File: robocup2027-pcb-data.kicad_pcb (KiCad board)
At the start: 6 copper layers, 83 x 117 mm, 51 parts, among them M5 Motor_Servo, M6 Motor_Servo, Q1 BPW40, Q2 BPW40, U1 ESP32-DEVKITC-32E

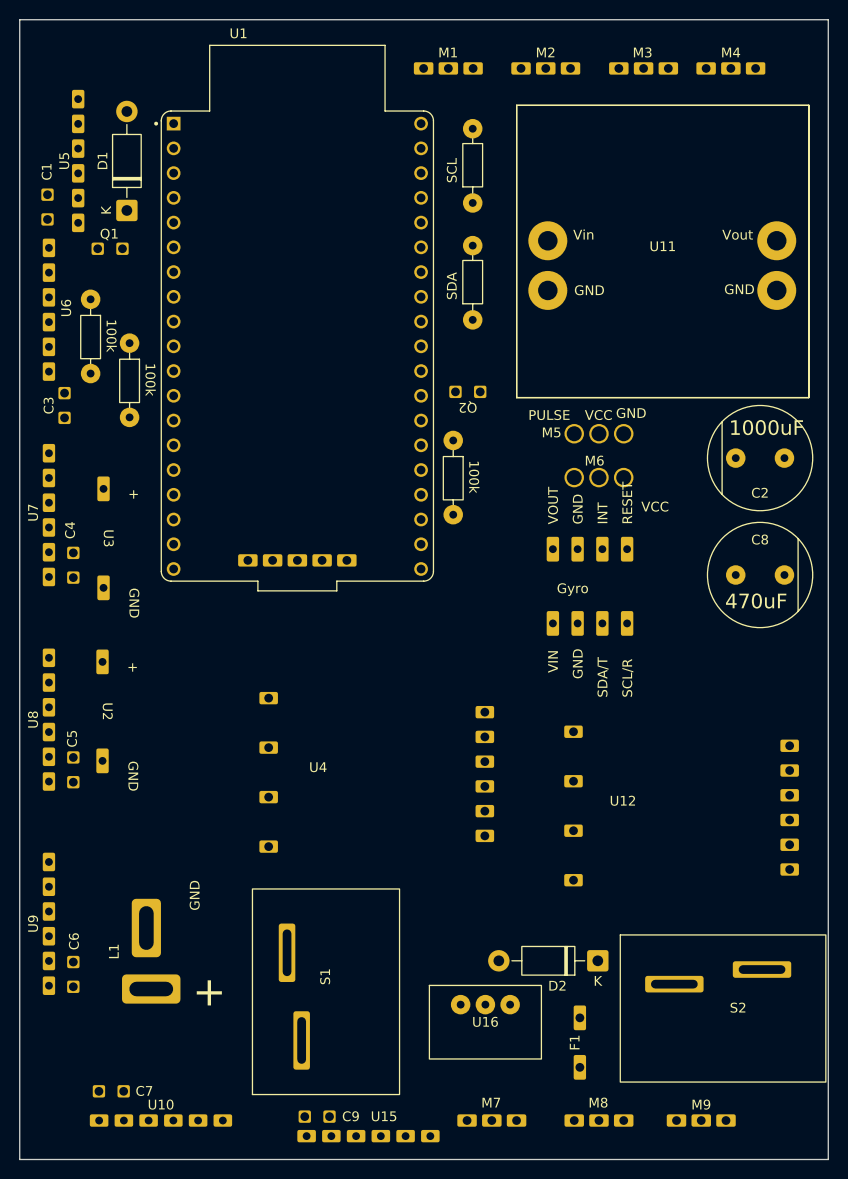
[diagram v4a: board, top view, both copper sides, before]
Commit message: add debug speaker
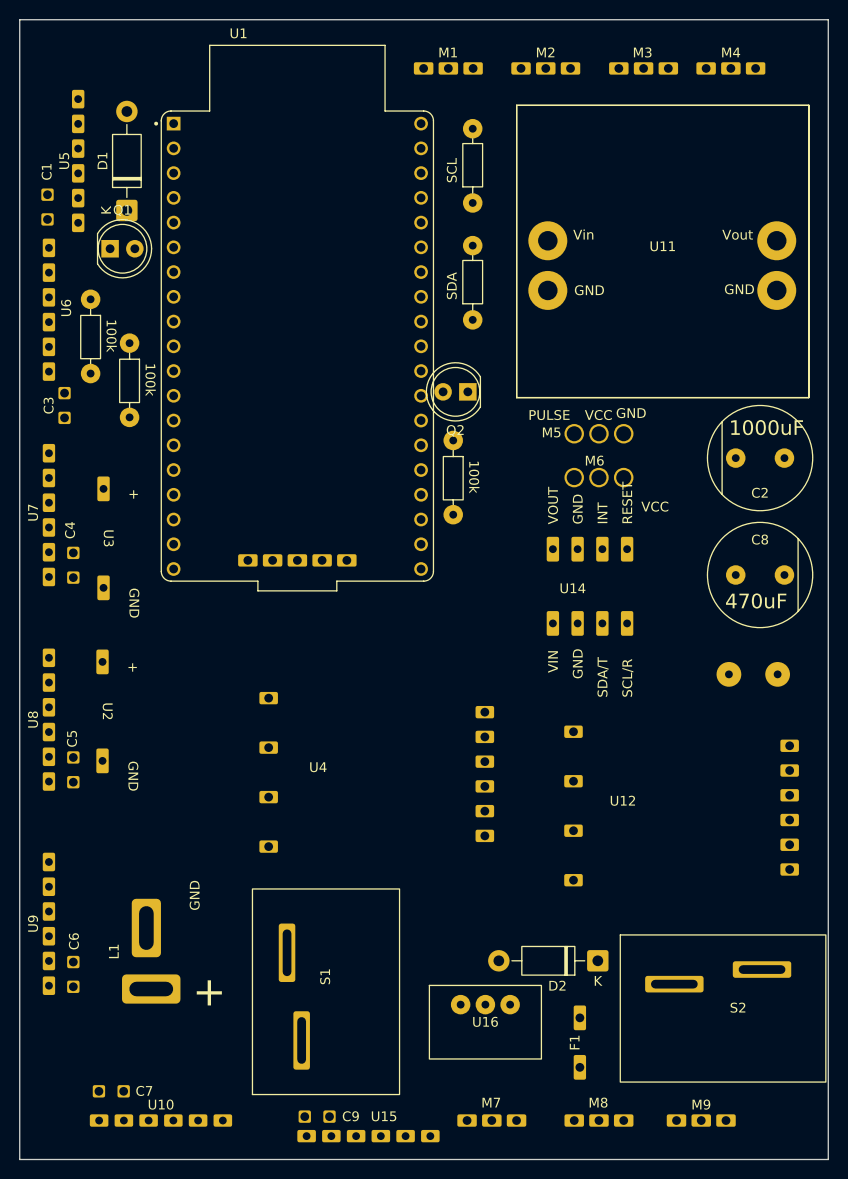
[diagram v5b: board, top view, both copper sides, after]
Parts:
- added U17: ~, robo:PKM13EPYH4000-A0, B.Cu at (165.3, 100.2)
- Q1, Q2: footprint robo:2.54mm_capacitor -> LED_THT:LED_D5.0mm_Clear
- renumbered Gyro to U14
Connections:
- U1 pad J3_15: unconnected-(U1-IO2-PadJ3_15) -> Debug

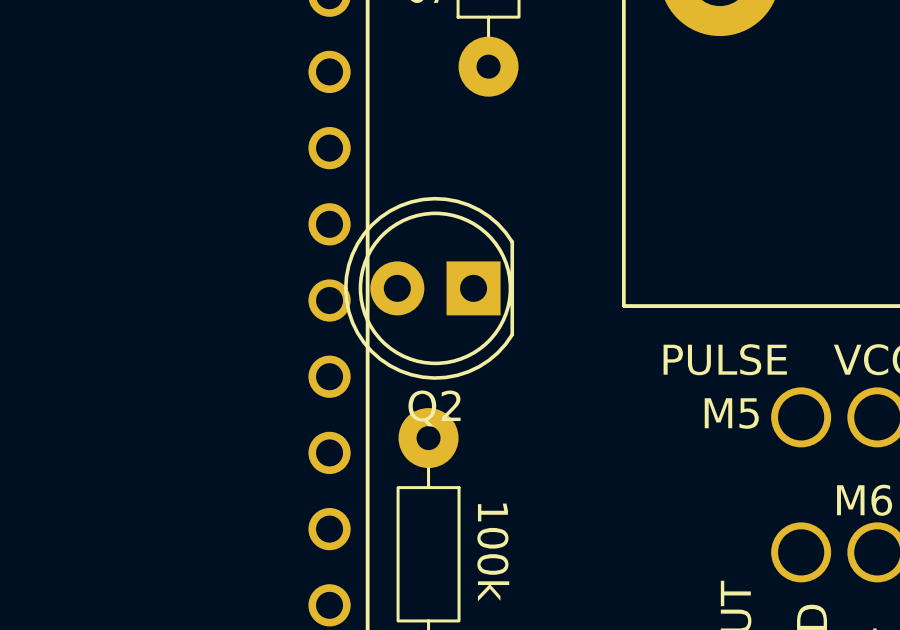
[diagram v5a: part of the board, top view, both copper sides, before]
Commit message: replaced photoreflector
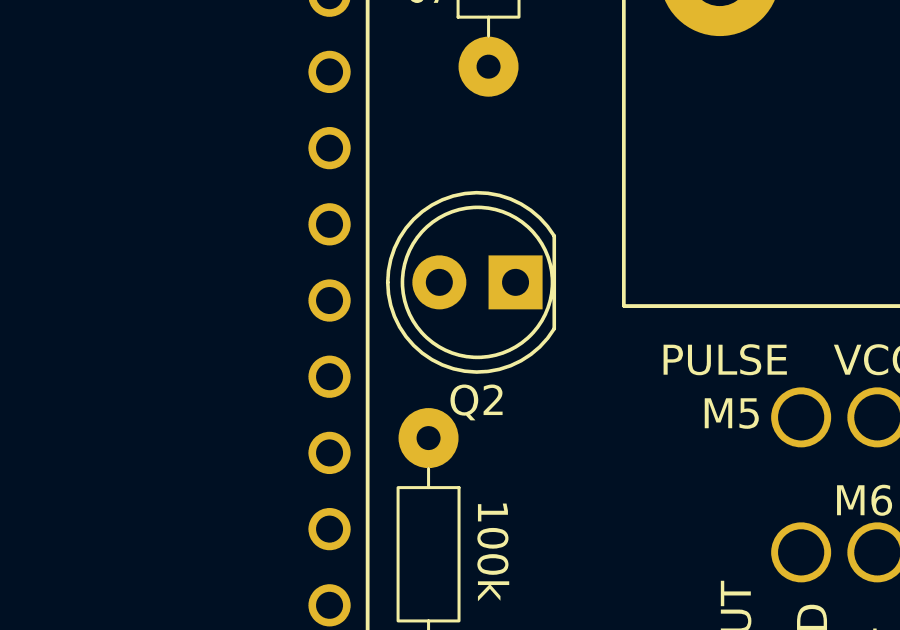
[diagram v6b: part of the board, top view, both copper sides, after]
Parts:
- moved Q2 1.41 mm to (137.4, 71.0)
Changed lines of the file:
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@@
 	(footprint "LED_THT:LED_D5.0mm_Clear"
 		(layer "F.Cu")
-		(at 136 71.2 180)
+		(at 137.4 71 180)
 		(descr "LED, diameter 5.0mm, 2 pins, clear, http://cdn-reichelt.de/documents/datenblatt/A500/LL-504BC2E-009.pdf, generated by kicad-footprint-generator")
 		(tags "LED")

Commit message: finished tracing
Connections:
- U13 pad 3: +5V -> +3.3V
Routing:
- net XSHUT5: track 0.00 -> 281.4 mm
- net I2C_SCL: track 0.00 -> 250.2 mm
- net I2C_SDA: track 0.00 -> 225.2 mm
- net LiPo+: track 0.00 -> 203.1 mm
- net STS3032_signal: track 0.00 -> 167.1 mm
- net Net-(U1-IO25): track 0.00 -> 152.7 mm
- net XSHUT4: track 0.00 -> 145.4 mm
- net XSHUT6: track 0.00 -> 128.7 mm
- net +5V: track 0.00 -> 108.9 mm
- net load2_CLK: track 0.00 -> 107.7 mm
- net load2_DAT: track 0.00 -> 96.8 mm
- net SG90_2_SIG: track 0.00 -> 95.3 mm
- net SG90_1_SIG: track 0.00 -> 93.5 mm
- net XSHUT3: track 0.00 -> 79.6 mm
- net load1_CLK: track 0.00 -> 63.5 mm
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- added copper zone on In3.Cu, net +3.3V
- added copper zone on In4.Cu, net +6V
- added copper zone on B.Cu, net GND

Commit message: refactor
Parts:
- moved U3 53.9 mm to (136.0, 125.1), turned to 0 degrees
- moved U17 4.30 mm to (161.4, 102.0), turned to 0 degrees
- moved M7 1.50 mm to (140.0, 146.0)
- moved D2 0.95 mm to (150.2, 129.2)
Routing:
- net XSHUT5: track 281.4 -> 99.4 mm, vias 0 -> 1
- net LiPo+: track 203.1 -> 145.9 mm, vias 0 -> 5
- net Debug: track 44.8 -> 48.1 mm
- net Net-(D2-A): track 4.98 -> 8.11 mm
- net STS3032_signal: track 167.1 -> 165.6 mm
- net Net-(L1-+): track 48.2 -> 48.9 mm
